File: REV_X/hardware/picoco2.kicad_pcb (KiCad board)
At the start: 2 copper layers, 54 x 102.9 mm, 40 parts, among them J1 Conn_01x03_Female, J2 Micro_SD_Card, J3 Conn_01x03_Female, Q1 Q_NMOS_GDS, SW1 SW_Push, SW2 SW_Push, U1 PicoW, U2 scd30, U3 ssd1306, U4 PCF8523T, U5 MCP73831-2-OT, Y1 32KHz

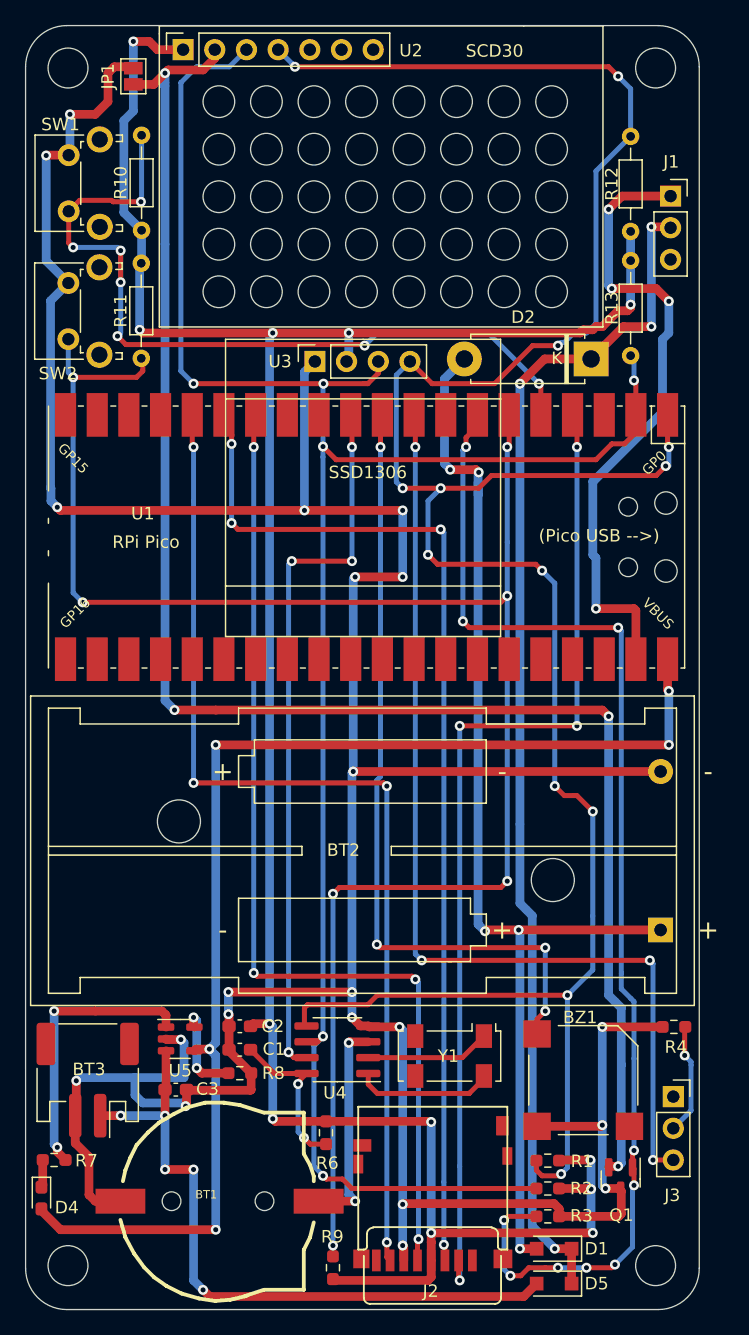
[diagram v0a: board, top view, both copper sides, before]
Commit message: add pico 3V3 and GND
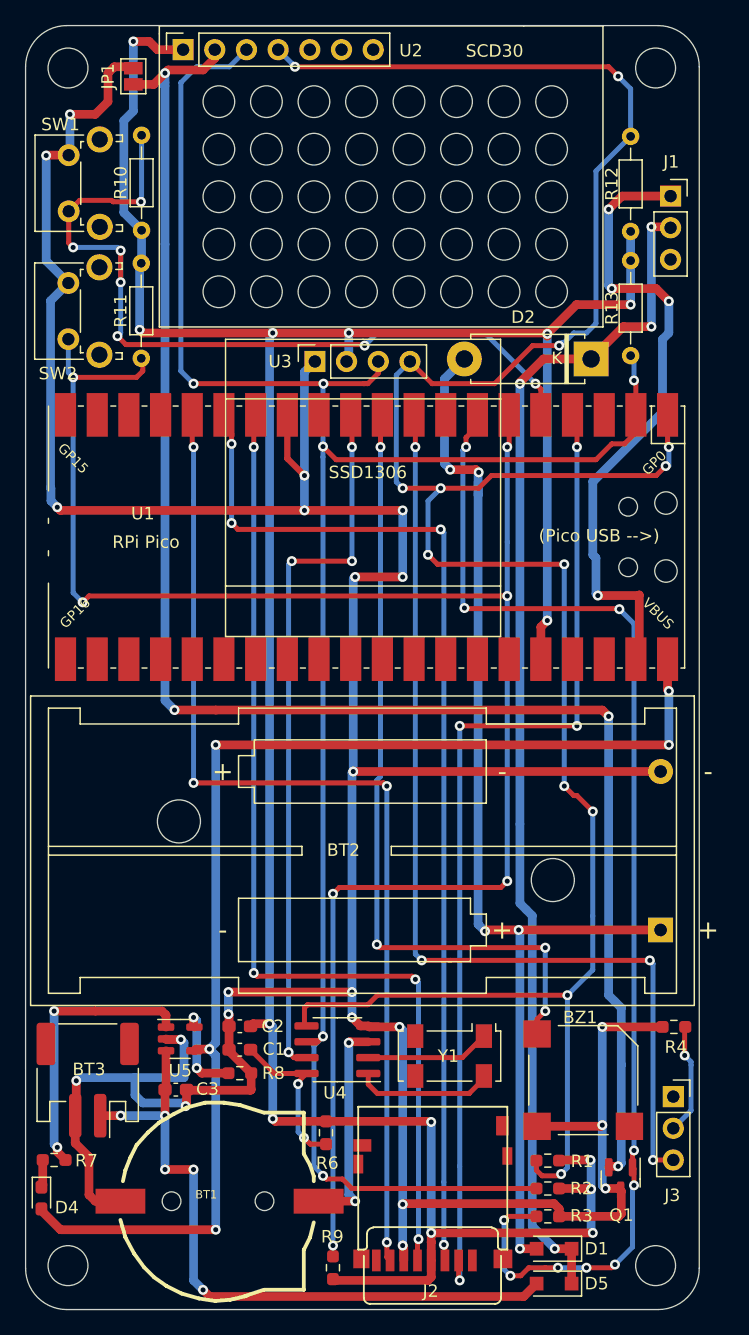
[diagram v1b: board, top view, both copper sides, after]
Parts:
- R4: value R -> 10K
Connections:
- U1 pad 13: unconnected-(U1-Pad13) -> GND
- U1 pad 36: unconnected-(U1-Pad36) -> +3V3
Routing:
- net +3V3: track 199.8 -> 225.3 mm, vias 12 -> 14
- net GND: track 276.5 -> 281.0 mm, vias 21 -> 22
- net SDA: track 196.5 -> 197.4 mm
